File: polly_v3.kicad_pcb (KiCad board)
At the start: 2 copper layers, 68.6 x 53.3 mm, 40 parts, among them J5 Conn_02x06_Odd_Even, P1 Power, P2 Analog, P3 Digital, P4 Digital, P5 CONN_01X01, P6 CONN_01X01, P7 CONN_01X01, P8 CONN_01X01, U1 4051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

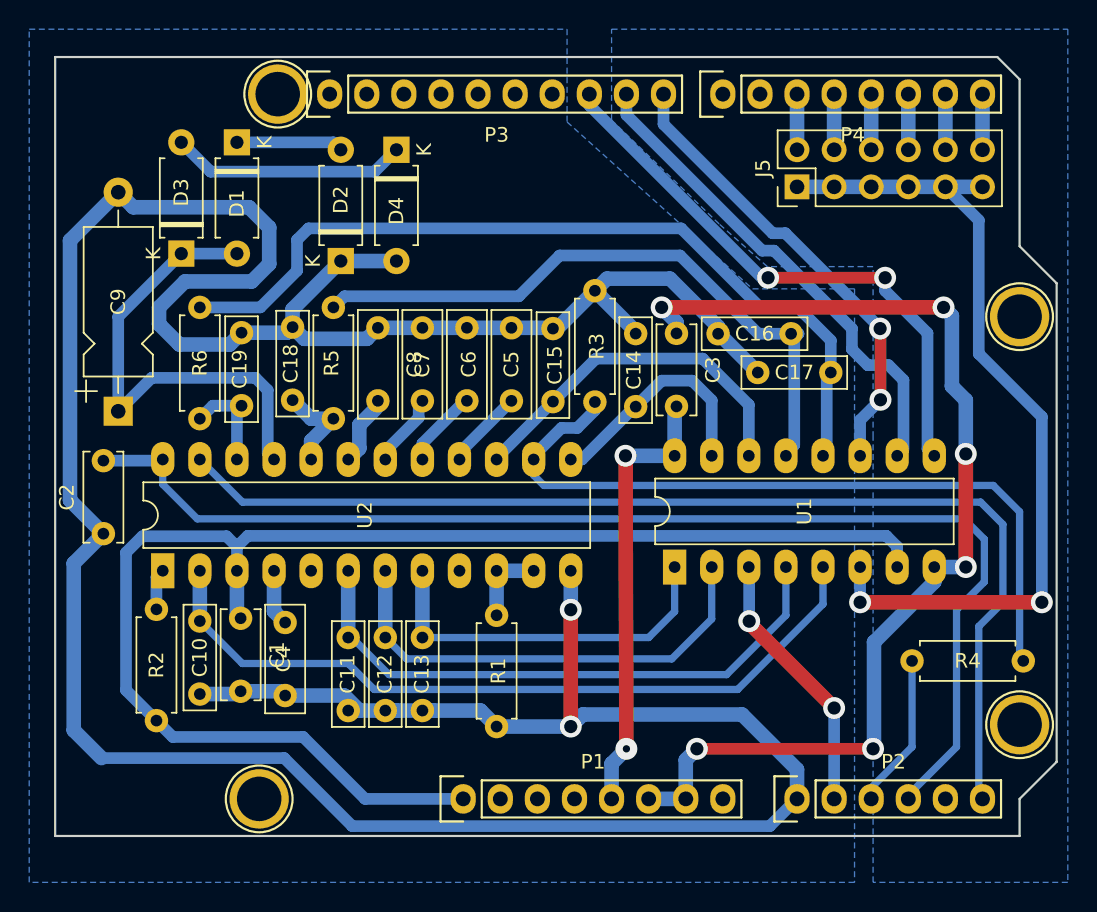
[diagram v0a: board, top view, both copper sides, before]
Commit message: Imporove layout for single sided, add previous versions
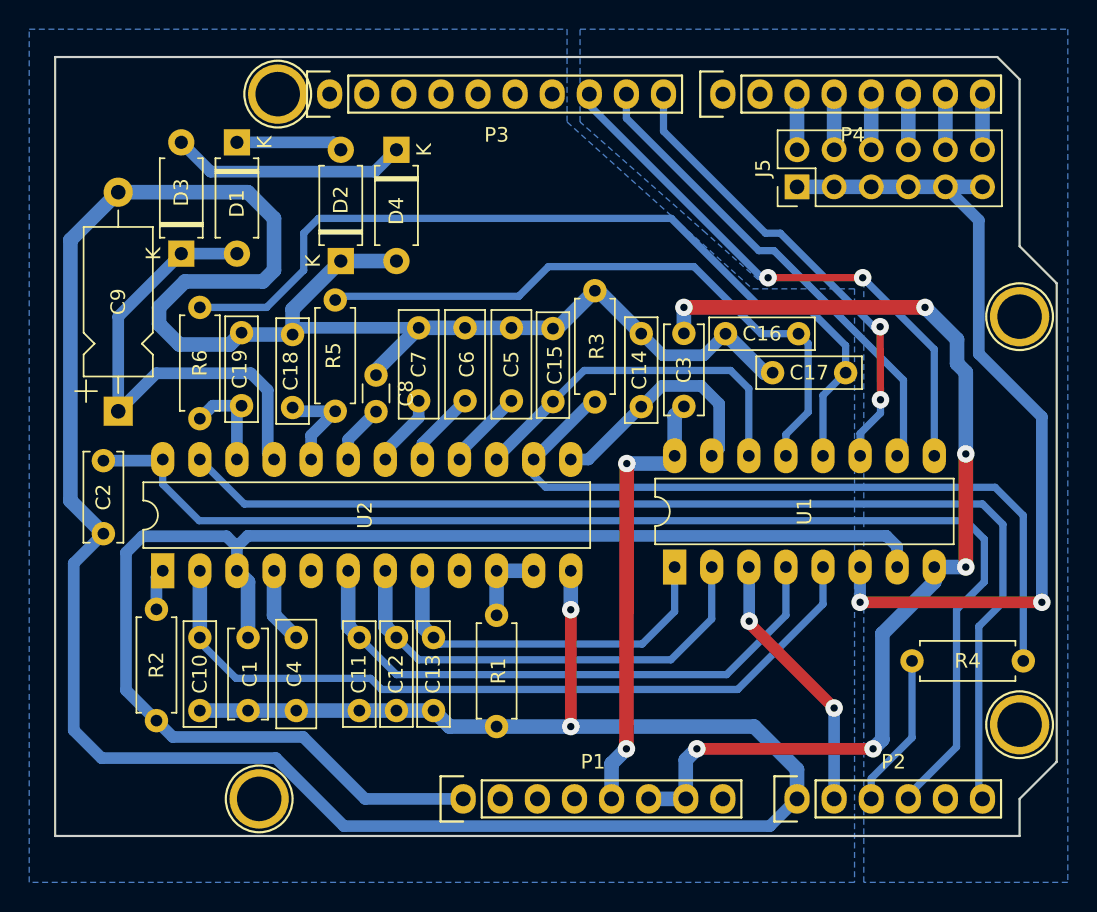
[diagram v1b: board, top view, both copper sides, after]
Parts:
- C8: footprint Capacitor_THT:C_Rect_L7.2mm_W2.5mm_P5.00mm_FKS2_FKP2_MKS2_MKP2 -> Capacitor_THT:C_Disc_D3.0mm_W1.6mm_P2.50mm
- moved C8 3.24 mm to (133.0, 94.8)
- moved C1 1.42 mm to (124.2, 112.8)
- moved C4 1.28 mm to (127.5, 112.8)
- moved C10 1.13 mm to (120.9, 112.8)
- moved C17 1.02 mm to (165.1, 94.6)
- moved C11 0.76 mm to (131.8, 112.8)
- moved C12 0.76 mm to (134.4, 112.8)
- moved C13 0.76 mm to (136.9, 112.8)
- moved R5 0.52 mm to (130.2, 97.3)
- moved C18 0.51 mm to (127.3, 97.0)
- moved C16 0.51 mm to (161.9, 92.0)
- moved C3 0.51 mm to (154.1, 91.9)
- moved C14 0.38 mm to (151.1, 97.0)
- moved C7 0.25 mm to (135.9, 91.6)
- moved C6 0.13 mm to (139.1, 91.6)
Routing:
- net /VCO_CV: track 53.0 -> 58.4 mm
- net GND: track 74.6 -> 71.9 mm
- net /VCA_CV: track 58.0 -> 60.0 mm
- net VEE: track 96.2 -> 97.7 mm
- net Net-(C4-Pad1): track 3.86 -> 5.20 mm
- net /LP_VCA_CV: track 7.04 -> 8.12 mm
- net /PARAM_SEL_A: track 39.5 -> 38.6 mm
- net GNDA: track 234.5 -> 235.4 mm
- net /PARAM_SEL_B: track 34.1 -> 33.4 mm
- net /MOD_AMT: track 40.8 -> 40.1 mm
